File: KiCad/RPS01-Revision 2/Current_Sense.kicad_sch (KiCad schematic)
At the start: 7 parts, among them U8 INA139QPWRQ1

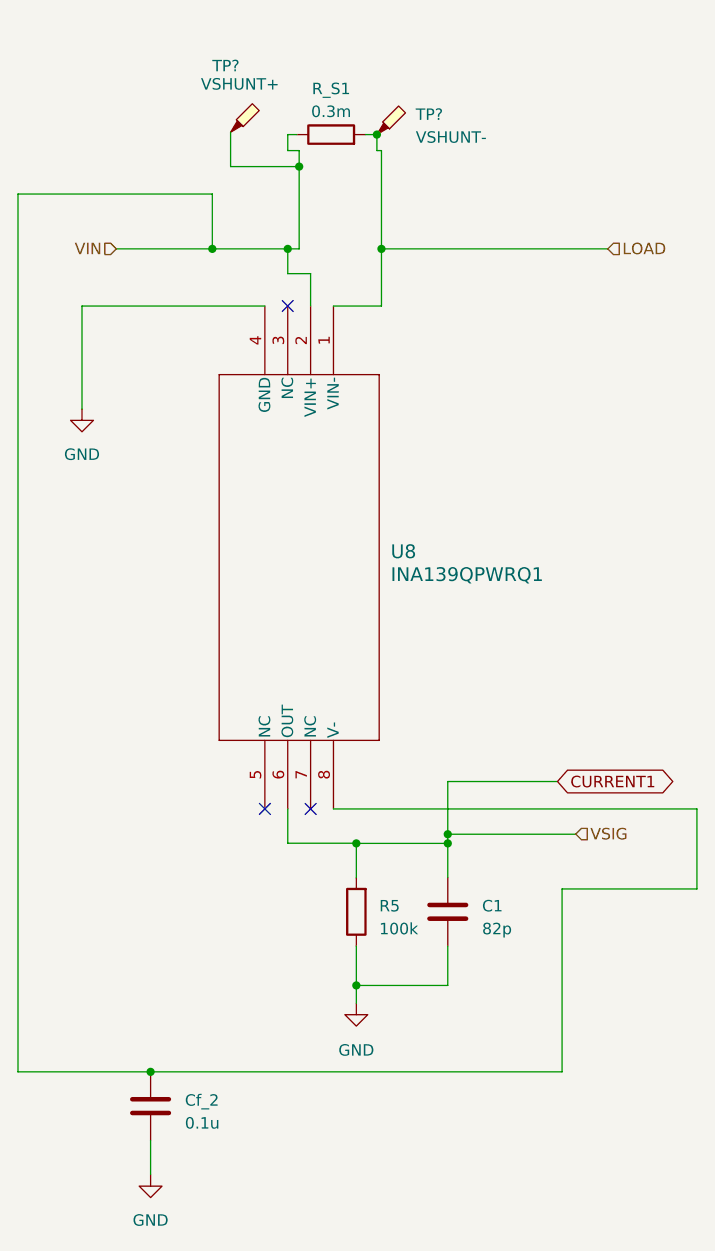
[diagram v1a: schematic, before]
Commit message: Current sense update
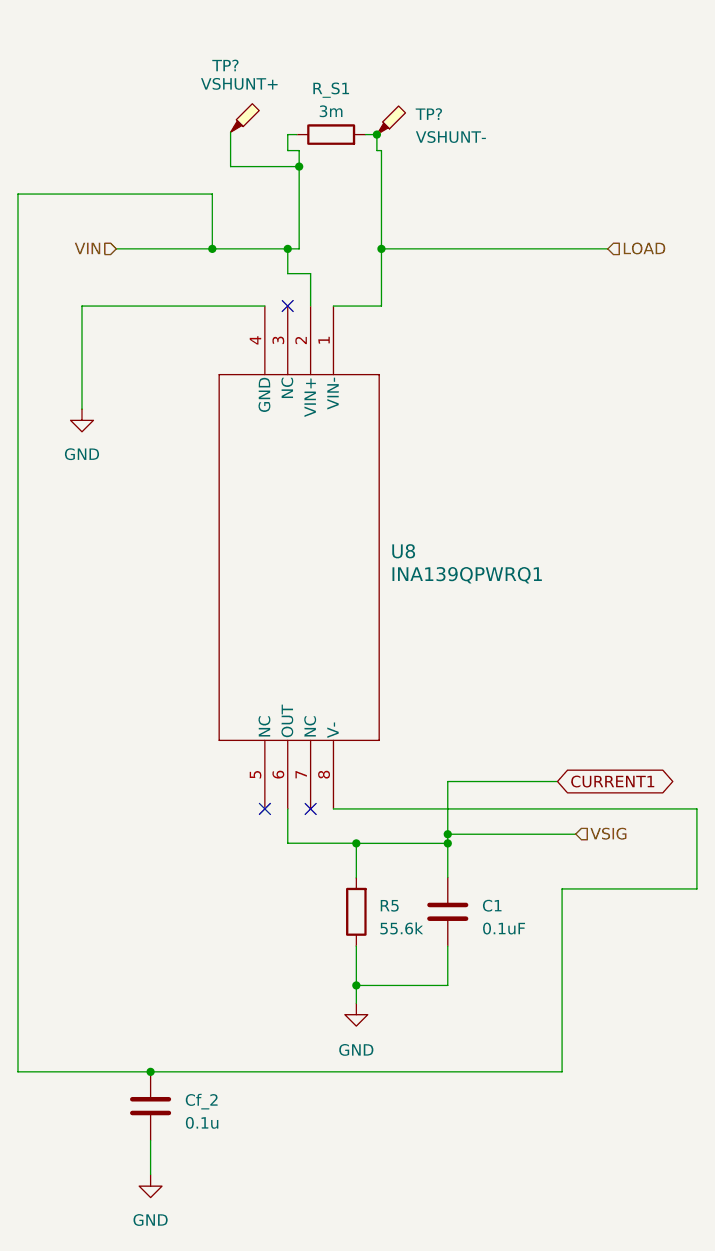
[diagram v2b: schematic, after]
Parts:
- C1: value 82p -> 0.1uF
- R5: value 100k -> 55.6k
- R_S1: value 0.3m -> 3m
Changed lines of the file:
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@@
       (effects (font (size 1.27 1.27)))
     )
-    (property "Value" "0.3m" (at 108.966 20.32 90)
+    (property "Value" "3m" (at 108.966 20.32 90)
       (effects (font (size 1.27 1.27)))
     )
@@
       (effects (font (size 1.27 1.27)) (justify left))
     )
-    (property "Value" "82p" (at 125.73 111.125 0)
+    (property "Value" "0.1uF" (at 125.73 111.125 0)
       (effects (font (size 1.27 1.27)) (justify left))
     )
@@
       (effects (font (size 1.27 1.27)) (justify right))
     )
-    (property "Value" "100k" (at 114.3 111.125 0)
+    (property "Value" "55.6k" (at 114.3 111.125 0)
       (effects (font (size 1.27 1.27)) (justify right))
     )

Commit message: Update Current sense references
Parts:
- R1_CS1: renamed from R5; value 55.6k -> 150k
- R_S1: value 3m -> 0.3m
- renumbered C1 to C1_CS1, Cf_2 to C2_CS1
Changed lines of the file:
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@@
       (effects (font (size 1.27 1.27)))
     )
-    (property "Value" "3m" (at 108.966 20.32 90)
+    (property "Value" "0.3m" (at 108.966 20.32 90)
       (effects (font (size 1.27 1.27)))
     )
@@
   (symbol (lib_id "Device:C") (at 121.92 109.22 0) (unit 1)
     (in_bom yes) (on_board yes) (dnp no) (fields_autoplaced)
-    (property "Reference" "C1" (at 125.73 108.585 0)
+    (property "Reference" "C1_CS1" (at 125.73 108.585 0)
       (effects (font (size 1.27 1.27)) (justify left))
     )
@@
       (project "rps01"
         (path "/14930f15-c0a0-4b55-93e6-b112548415f6/13e150ee-6c46-47a5-9c09-3749eb0dcbfe"
-          (reference "C1") (unit 1)
+          (reference "C1_CS1") (unit 1)
         )
       )
@@
   (symbol (lib_id "Device:C") (at 88.9 130.81 0) (unit 1)
     (in_bom yes) (on_board yes) (dnp no) (fields_autoplaced)
-    (property "Reference" "Cf_2" (at 92.71 130.175 0)
+    (property "Reference" "C2_CS1" (at 92.71 130.175 0)
       (effects (font (size 1.27 1.27)) (justify left))
     )
@@
       (project "rps01"
         (path "/14930f15-c0a0-4b55-93e6-b112548415f6/13e150ee-6c46-47a5-9c09-3749eb0dcbfe"
-          (reference "Cf_2") (unit 1)
+          (reference "C2_CS1") (unit 1)
         )
         (path "/14930f15-c0a0-4b55-93e6-b112548415f6/83d3dc76-6aeb-422d-8708-14a32de244f0"
@@
   (symbol (lib_id "Device:R") (at 111.76 109.22 180) (unit 1)
     (in_bom yes) (on_board yes) (dnp no) (fields_autoplaced)
-    (property "Reference" "R5" (at 114.3 108.585 0)
+    (property "Reference" "R1_CS1" (at 114.3 108.585 0)
       (effects (font (size 1.27 1.27)) (justify right))
     )
-    (property "Value" "55.6k" (at 114.3 111.125 0)
+    (property "Value" "150k" (at 114.3 111.125 0)
       (effects (font (size 1.27 1.27)) (justify right))
     )
@@
       (project "rps01"
         (path "/14930f15-c0a0-4b55-93e6-b112548415f6/13e150ee-6c46-47a5-9c09-3749eb0dcbfe"
-          (reference "R5") (unit 1)
+          (reference "R1_CS1") (unit 1)
         )
       )

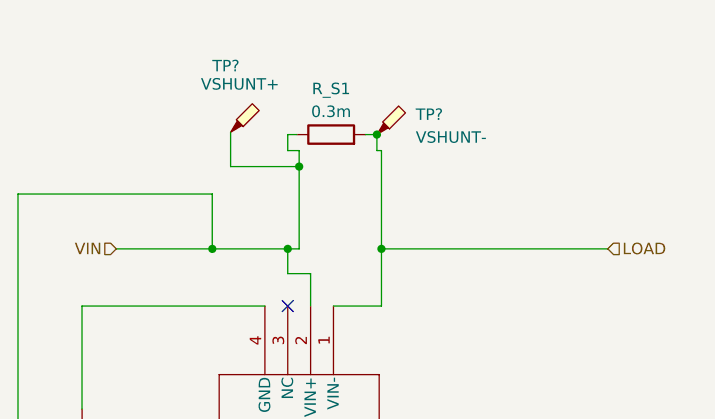
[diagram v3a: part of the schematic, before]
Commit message: Updated nets of Current 2 output and 3780 Globals.
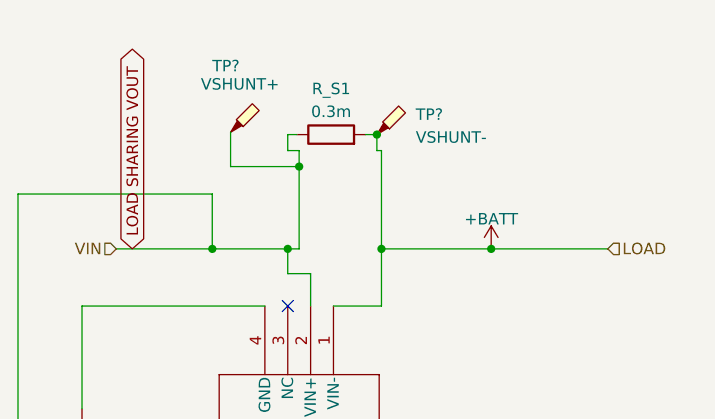
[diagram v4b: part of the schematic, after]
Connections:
- net LOAD renamed +BATT
- net VIN renamed LOAD SHARING VOUT
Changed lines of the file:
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@@
   (junction (at 105.41 26.416) (diameter 0) (color 0 0 0 0)
   )
+  (junction (at 126.746 35.56) (diameter 0) (color 0 0 0 0)
+  )
   (junction (at 95.758 35.56) (diameter 0) (color 0 0 0 0)
   )
@@
     (stroke (width 0) (type default))
   )
-  (wire (pts (xy 114.554 35.56) (xy 139.7 35.56))
+  (wire (pts (xy 114.554 35.56) (xy 126.746 35.56))
     (stroke (width 0) (type default))
   )
@@
     (stroke (width 0) (type default))
   )
+  (wire (pts (xy 126.746 35.56) (xy 139.7 35.56))
+    (stroke (width 0) (type default))
+  )
   (wire (pts (xy 104.14 101.6) (xy 111.76 101.6))
     (stroke (width 0) (type default))
@@
     )
   )
+  (global_label "LOAD SHARING VOUT" (shape bidirectional) (at 86.868 35.56 90) (fields_autoplaced)
+    (effects (font (size 1.27 1.27)) (justify left))
+    (property "Intersheetrefs" "${INTERSHEET_REFS}" (at 86.868 12.0694 90)
+      (effects (font (size 1.27 1.27)) (justify left) hide)
+    )
+  )
   (global_label "CURRENT1" (shape bidirectional) (at 134.112 94.742 0) (fields_autoplaced)
     (effects (font (size 1.27 1.27)) (justify left))
@@
     (effects (font (size 1.27 1.27)) (justify right))
   )
+  (symbol (lib_id "power:+BATT") (at 126.746 35.56 0) (unit 1)
+    (in_bom yes) (on_board yes) (dnp no) (fields_autoplaced)
+    (property "Reference" "#PWR03" (at 126.746 39.37 0)
+      (effects (font (size 1.27 1.27)) hide)
+    )
+    (property "Value" "+BATT" (at 126.746 32.258 0)
+      (effects (font (size 1.27 1.27)))
+    )
+    (property "Footprint" "" (at 126.746 35.56 0)
+      (effects (font (size 1.27 1.27)) hide)
+    )
+    (property "Datasheet" "" (at 126.746 35.56 0)
+      (effects (font (size 1.27 1.27)) hide)
+    )
+    (pin "1")
+    (instances
+      (project "rps01"
+        (path "/14930f15-c0a0-4b55-93e6-b112548415f6"
+          (reference "#PWR03") (unit 1)
+        )
+        (path "/14930f15-c0a0-4b55-93e6-b112548415f6/13e150ee-6c46-47a5-9c09-3749eb0dcbfe"
+          (reference "#PWR027") (unit 1)
+        )
+      )
+    )
+  )
   (symbol (lib_id "Connector:TestPoint_Probe") (at 114.046 22.86 0) (unit 1)
